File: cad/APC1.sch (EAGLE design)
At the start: 27 parts, among them IC1 LM555N, IC2 LM555N

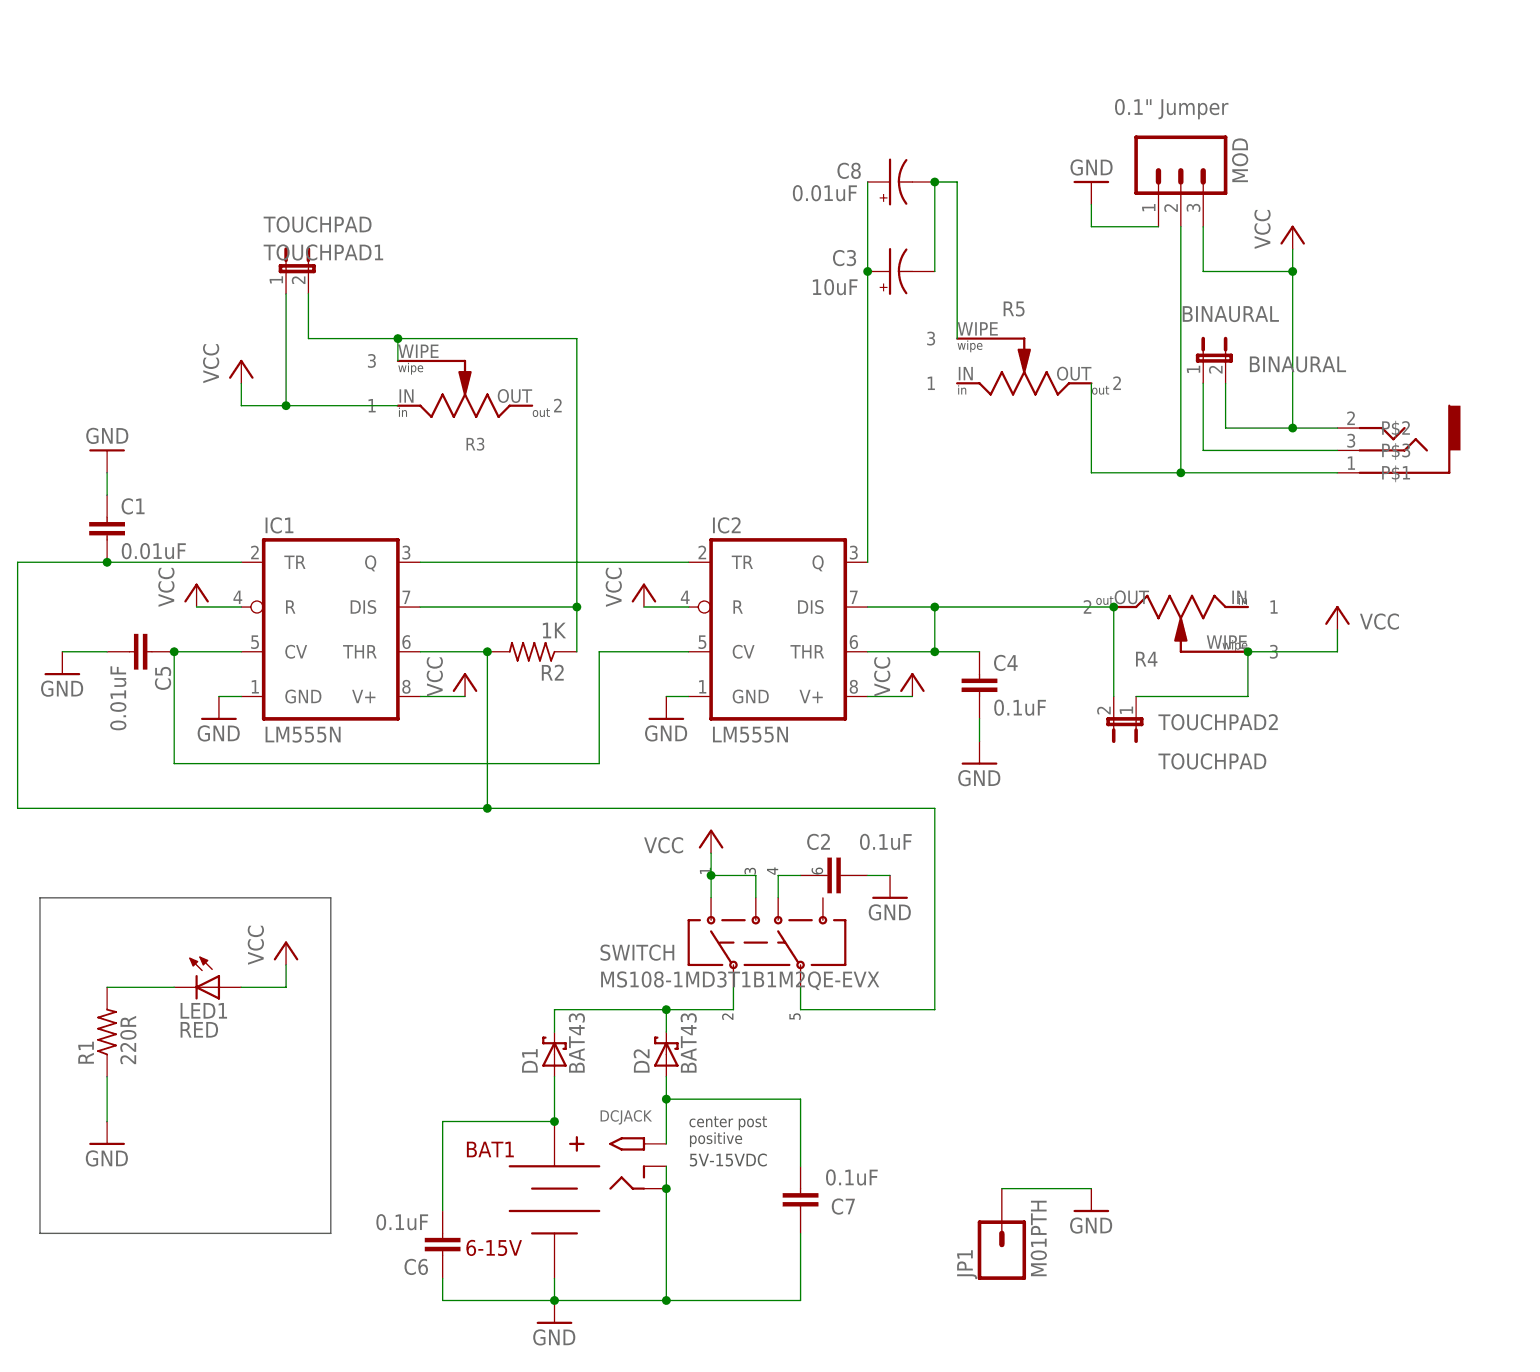
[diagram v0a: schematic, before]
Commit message: Fixed wiring on pots; more careful routing I had changed the schematic for two pots incorrectly, volume and pulse width. Added two current-limiting resistors for the freq. and pulse width pots. Spent more time with the trace routing. Eliminated a few vias. Widened trace widths and spread out traces to enable (at least potentially) desktop CNC PCB routing, such as with an OtherMill Pro. Changed some of the documentation and many of the images too, naturally. Also changed the .gitignore file to reflect more careful cataloging of the important parts of the project.
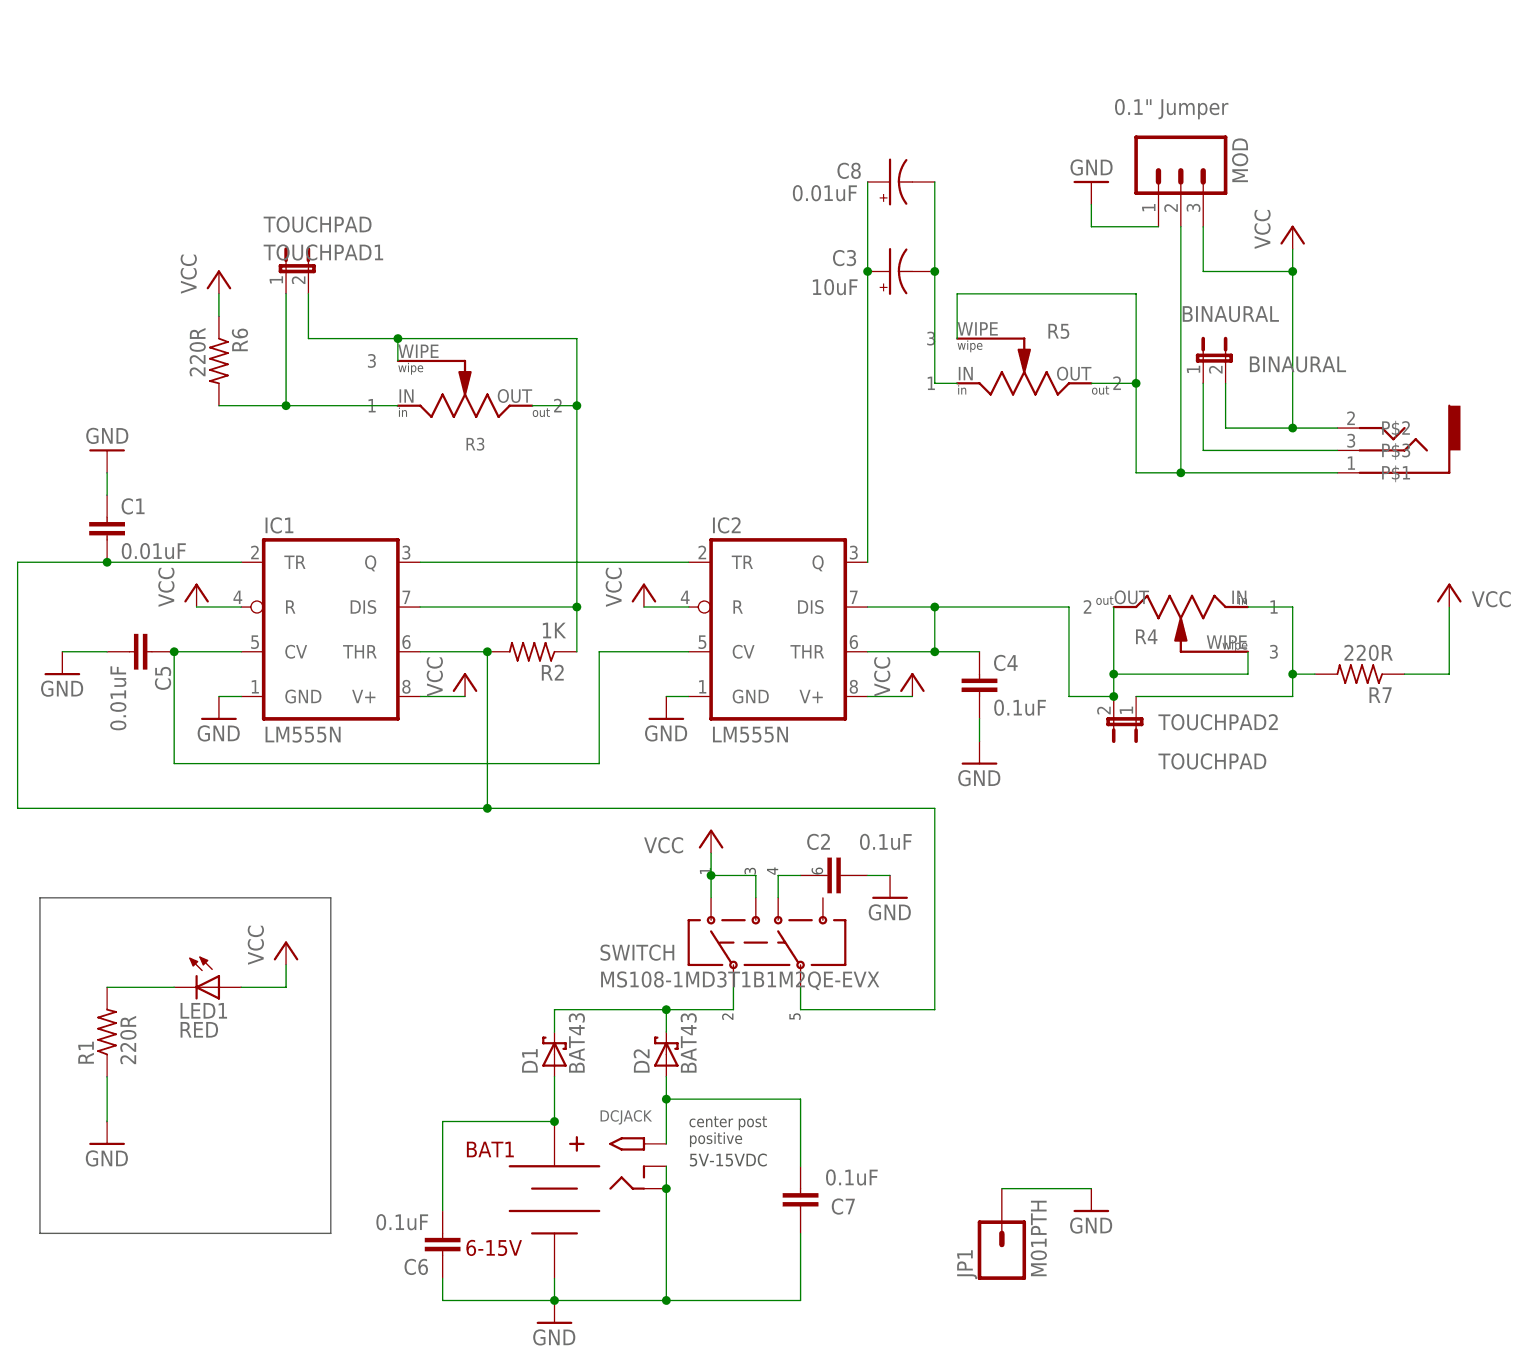
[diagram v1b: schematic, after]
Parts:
- added R6, R7: 220R, rcl:R-US_0207/7
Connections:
- new net N$13: LINE.P$1, MOD.2, R5.2, R5.3
- new net N$15: R3.1, R6.2, TOUCHPAD1.1
- net N$1: now also R3.2
- net N$14: now also R4.1, R7.2, TOUCHPAD2.1; no longer LINE.P$1, MOD.2, R5.2
- net N$16: now also R5.1; no longer R5.3
- net N$3: now also R4.3
- net VCC: now also R6.1, R7.1; no longer R3.1, R4.3, TOUCHPAD1.1, TOUCHPAD2.1
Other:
- note added: "Isolate from DC"
- note added: "These 220R resistors are probably unnecessary current-limiters in series with the rotary pots."
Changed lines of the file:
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@@
 <part name="JP1" library="SparkFun-Connectors" deviceset="M01" device="PTH"/>
 <part name="GND7" library="SparkFun-Aesthetics" deviceset="GND" device=""/>
+<part name="R6" library="rcl" deviceset="R-US_" device="0207/7" value="220R"/>
+<part name="R7" library="rcl" deviceset="R-US_" device="0207/7" value="220R"/>
 </parts>
 <sheets>
@@
 switch design that may
 be implemented later.</text>
+<text x="83.82" y="134.62" size="1.778" layer="98">Isolate from DC</text>
+<text x="5.08" y="132.08" size="1.778" layer="98" font="vector" ratio="10">These 220R resistors
+are probably unnecessary
+current-limiters in series
+with the rotary pots.</text>
 </plain>
 <instances>
@@
 <instance part="DCJACK" gate="G$1" x="66.04" y="17.78"/>
 <instance part="R5" gate="R$1" x="111.76" y="106.68" smashed="yes">
-<attribute name="NAME" x="109.22" y="114.3" size="1.6764" layer="95" font="vector"/>
+<attribute name="NAME" x="114.3" y="111.76" size="1.6764" layer="95" font="vector"/>
 <attribute name="VALUE" x="109.22" y="101.6" size="1.6764" layer="96" font="vector"/>
 </instance>
@@
 </instance>
 <instance part="R4" gate="R$1" x="129.54" y="81.28" smashed="yes" rot="R180">
-<attribute name="NAME" x="127" y="76.2" size="1.6764" layer="95" font="vector" rot="R180"/>
+<attribute name="NAME" x="127" y="78.74" size="1.6764" layer="95" font="vector" rot="R180"/>
 <attribute name="VALUE" x="132.08" y="86.36" size="1.6764" layer="96" font="vector" rot="R180"/>
 </instance>
 <instance part="P+1" gate="VCC" x="99.06" y="73.66"/>
 <instance part="P+2" gate="VCC" x="48.26" y="73.66"/>
-<instance part="P+3" gate="VCC" x="22.86" y="109.22"/>
+<instance part="P+3" gate="VCC" x="20.32" y="119.38"/>
 <instance part="GND1" gate="1" x="20.32" y="68.58"/>
 <instance part="GND2" gate="1" x="71.12" y="68.58"/>
-<instance part="P+4" gate="VCC" x="147.32" y="81.28" smashed="yes">
-<attribute name="VALUE" x="149.86" y="78.74" size="1.778" layer="96"/>
+<instance part="P+4" gate="VCC" x="160.02" y="83.82" smashed="yes">
+<attribute name="VALUE" x="162.56" y="81.28" size="1.778" layer="96"/>
 </instance>
 <instance part="GND3" gate="1" x="96.52" y="48.26"/>
@@
 <instance part="JP1" gate="G$1" x="109.22" y="7.62" rot="R90"/>
 <instance part="GND7" gate="1" x="119.38" y="12.7"/>
+<instance part="R6" gate="G$1" x="20.32" y="109.22" rot="R270"/>
+<instance part="R7" gate="G$1" x="149.86" y="73.66" rot="R180"/>
 </instances>
 <busses>
@@
 <pinref part="IC1" gate="A" pin="DIS"/>
 <wire x1="43.18" y1="81.28" x2="60.96" y2="81.28" width="0.1524" layer="91"/>
-<wire x1="60.96" y1="111.76" x2="60.96" y2="81.28" width="0.1524" layer="91"/>
+<wire x1="60.96" y1="111.76" x2="60.96" y2="104.14" width="0.1524" layer="91"/>
 <junction x="60.96" y="81.28"/>
 <pinref part="R3" gate="R$1" pin="3"/>
+<wire x1="60.96" y1="104.14" x2="60.96" y2="81.28" width="0.1524" layer="91"/>
 <wire x1="40.64" y1="109.22" x2="40.64" y2="111.76" width="0.1524" layer="91"/>
 <wire x1="40.64" y1="111.76" x2="60.96" y2="111.76" width="0.1524" layer="91"/>
@@
 <wire x1="30.48" y1="111.76" x2="40.64" y2="111.76" width="0.1524" layer="91"/>
 <junction x="40.64" y="111.76"/>
+<pinref part="R3" gate="R$1" pin="2"/>
+<wire x1="55.88" y1="104.14" x2="60.96" y2="104.14" width="0.1524" layer="91"/>
+<junction x="60.96" y="104.14"/>
 </segment>
 </net>
@@
 <segment>
 <pinref part="P+3" gate="VCC" pin="VCC"/>
-<pinref part="R3" gate="R$1" pin="1"/>
-<wire x1="22.86" y1="106.68" x2="22.86" y2="104.14" width="0.1524" layer="91"/>
-<wire x1="22.86" y1="104.14" x2="27.94" y2="104.14" width="0.1524" layer="91"/>
-<pinref part="TOUCHPAD1" gate="A" pin="1"/>
-<wire x1="27.94" y1="104.14" x2="40.64" y2="104.14" width="0.1524" layer="91"/>
-<wire x1="27.94" y1="116.84" x2="27.94" y2="104.14" width="0.1524" layer="91"/>
-<junction x="27.94" y="104.14"/>
+<wire x1="20.32" y1="116.84" x2="20.32" y2="114.3" width="0.1524" layer="91"/>
+<pinref part="R6" gate="G$1" pin="1"/>
 </segment>
 <segment>
 <pinref part="P+4" gate="VCC" pin="VCC"/>
-<pinref part="R4" gate="R$1" pin="3"/>
-<wire x1="137.16" y1="76.2" x2="147.32" y2="76.2" width="0.1524" layer="91"/>
-<wire x1="147.32" y1="76.2" x2="147.32" y2="78.74" width="0.1524" layer="91"/>
-<pinref part="TOUCHPAD2" gate="A" pin="1"/>
-<wire x1="124.46" y1="71.12" x2="137.16" y2="71.12" width="0.1524" layer="91"/>
-<wire x1="137.16" y1="71.12" x2="137.16" y2="76.2" width="0.1524" layer="91"/>
-<junction x="137.16" y="76.2"/>
+<pinref part="R7" gate="G$1" pin="1"/>
+<wire x1="154.94" y1="73.66" x2="160.02" y2="73.66" width="0.1524" layer="91"/>
+<wire x1="160.02" y1="73.66" x2="160.02" y2="81.28" width="0.1524" layer="91"/>
 </segment>
 <segment>
@@
 </segment>
 </net>
-<net name="N$14" class="0">
-<segment>
-<pinref part="LINE" gate="G$1" pin="P$1"/>
-<wire x1="129.54" y1="96.52" x2="119.38" y2="96.52" width="0.1524" layer="91"/>
-<wire x1="147.32" y1="96.52" x2="129.54" y2="96.52" width="0.1524" layer="91"/>
-<wire x1="129.54" y1="124.46" x2="129.54" y2="96.52" width="0.1524" layer="91"/>
-<junction x="129.54" y="96.52"/>
-<pinref part="MOD" gate="G$1" pin="2"/>
-<pinref part="R5" gate="R$1" pin="2"/>
-<wire x1="119.38" y1="96.52" x2="119.38" y2="106.68" width="0.1524" layer="91"/>
-</segment>
-</net>
 <net name="N$7" class="0">
 <segment>
@@
 <pinref part="IC2" gate="A" pin="DIS"/>
 <wire x1="93.98" y1="81.28" x2="101.6" y2="81.28" width="0.1524" layer="91"/>
-<junction x="101.6" y="81.28"/>
-<pinref part="R4" gate="R$1" pin="2"/>
-<wire x1="121.92" y1="81.28" x2="101.6" y2="81.28" width="0.1524" layer="91"/>
 <wire x1="101.6" y1="76.2" x2="101.6" y2="81.28" width="0.1524" layer="91"/>
 <junction x="101.6" y="76.2"/>
@@
 <pinref part="IC2" gate="A" pin="THR"/>
 <wire x1="93.98" y1="76.2" x2="101.6" y2="76.2" width="0.1524" layer="91"/>
+<wire x1="101.6" y1="81.28" x2="116.84" y2="81.28" width="0.1524" layer="91"/>
+<wire x1="116.84" y1="81.28" x2="116.84" y2="71.12" width="0.1524" layer="91"/>
+<junction x="101.6" y="81.28"/>
 <pinref part="TOUCHPAD2" gate="A" pin="2"/>
-<wire x1="121.92" y1="81.28" x2="121.92" y2="71.12" width="0.1524" layer="91"/>
-<junction x="121.92" y="81.28"/>
+<wire x1="116.84" y1="71.12" x2="121.92" y2="71.12" width="0.1524" layer="91"/>
+<pinref part="R4" gate="R$1" pin="3"/>
+<wire x1="137.16" y1="76.2" x2="137.16" y2="73.66" width="0.1524" layer="91"/>
+<wire x1="137.16" y1="73.66" x2="121.92" y2="73.66" width="0.1524" layer="91"/>
+<wire x1="121.92" y1="73.66" x2="121.92" y2="71.12" width="0.1524" layer="91"/>
+<junction x="121.92" y="71.12"/>
+<pinref part="R4" gate="R$1" pin="2"/>
+<wire x1="121.92" y1="81.28" x2="121.92" y2="73.66" width="0.1524" layer="91"/>
+<junction x="121.92" y="73.66"/>
 </segment>
 </net>
 <net name="N$16" class="0">
 <segment>
-<wire x1="104.14" y1="111.76" x2="104.14" y2="129.54" width="0.1524" layer="91"/>
 <pinref part="C3" gate="G$1" pin="-"/>
 <pinref part="C8" gate="G$1" pin="-"/>
-<junction x="101.6" y="129.54"/>
 <wire x1="101.6" y1="129.54" x2="101.6" y2="119.38" width="0.1524" layer="91"/>
-<wire x1="104.14" y1="129.54" x2="101.6" y2="129.54" width="0.1524" layer="91"/>
-<pinref part="R5" gate="R$1" pin="3"/>
+<wire x1="101.6" y1="119.38" x2="101.6" y2="106.68" width="0.1524" layer="91"/>
+<junction x="101.6" y="119.38"/>
+<pinref part="R5" gate="R$1" pin="1"/>
+<wire x1="101.6" y1="106.68" x2="104.14" y2="106.68" width="0.1524" layer="91"/>
 </segment>
 </net>
@@
 </segment>
 </net>
+<net name="N$13" class="0">
+<segment>
+<pinref part="R5" gate="R$1" pin="3"/>
+<wire x1="104.14" y1="111.76" x2="104.14" y2="116.84" width="0.1524" layer="91"/>
+<wire x1="104.14" y1="116.84" x2="124.46" y2="116.84" width="0.1524" layer="91"/>
+<wire x1="124.46" y1="116.84" x2="124.46" y2="106.68" width="0.1524" layer="91"/>
+<pinref part="LINE" gate="G$1" pin="P$1"/>
+<wire x1="124.46" y1="106.68" x2="124.46" y2="96.52" width="0.1524" layer="91"/>
+<wire x1="147.32" y1="96.52" x2="129.54" y2="96.52" width="0.1524" layer="91"/>
+<wire x1="129.54" y1="124.46" x2="129.54" y2="96.52" width="0.1524" layer="91"/>
+<pinref part="MOD" gate="G$1" pin="2"/>
+<wire x1="124.46" y1="96.52" x2="129.54" y2="96.52" width="0.1524" layer="91"/>
+<junction x="129.54" y="96.52"/>
+<pinref part="R5" gate="R$1" pin="2"/>
+<wire x1="119.38" y1="106.68" x2="124.46" y2="106.68" width="0.1524" layer="91"/>
+<junction x="124.46" y="106.68"/>
+</segment>
+</net>
+<net name="N$14" class="0">
+<segment>
+<pinref part="TOUCHPAD2" gate="A" pin="1"/>
+<wire x1="124.46" y1="71.12" x2="142.24" y2="71.12" width="0.1524" layer="91"/>
+<pinref part="R4" gate="R$1" pin="1"/>
+<wire x1="137.16" y1="81.28" x2="142.24" y2="81.28" width="0.1524" layer="91"/>
+<wire x1="142.24" y1="81.28" x2="142.24" y2="73.66" width="0.1524" layer="91"/>
+<pinref part="R7" gate="G$1" pin="2"/>
+<wire x1="142.24" y1="73.66" x2="142.24" y2="71.12" width="0.1524" layer="91"/>
+<wire x1="144.78" y1="73.66" x2="142.24" y2="73.66" width="0.1524" layer="91"/>
+<junction x="142.24" y="73.66"/>
+</segment>
+</net>
+<net name="N$15" class="0">
+<segment>
+<pinref part="R3" gate="R$1" pin="1"/>
+<wire x1="20.32" y1="104.14" x2="27.94" y2="104.14" width="0.1524" layer="91"/>
+<pinref part="TOUCHPAD1" gate="A" pin="1"/>
+<wire x1="27.94" y1="104.14" x2="40.64" y2="104.14" width="0.1524" layer="91"/>
+<wire x1="27.94" y1="116.84" x2="27.94" y2="104.14" width="0.1524" layer="91"/>
+<junction x="27.94" y="104.14"/>
+<pinref part="R6" gate="G$1" pin="2"/>
+</segment>
+</net>

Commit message: v.1.2 of board. Documentation changes / improvements.
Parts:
- removed C7: 0.1uF, rcl:C-EU050-024X044
- removed C8: 0.01uF, rcl:CPOL-USE2.5-7
- added FREQUENCY: M04X2, SparkFun-Connectors:M04X2
- added JP2: FREQ_BYPASS, SparkFun-Connectors:M03SMD_RA_MALE
- C6: value 0.1uF -> 0.01uF; device rcl:C-EU050-024X044 -> rcl:CPOL-USE2.5-7
- R1: value 220R -> 470R
- renumbered LED1 to LED
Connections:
- net N$12 renamed VIN
- new net N$18: FREQUENCY.1, R6.2
- new net N$19: FREQUENCY.4, JP2.1, R3.1
- new net N$20: FREQUENCY.6, IC1.DIS, R2.1
- net GND: now also FREQUENCY.7, FREQUENCY.8; no longer C6.1, C7.1
- net N$1: now also FREQUENCY.5, JP2.2, JP2.3; no longer IC1.DIS, R2.1
- net N$10: no longer C6.2
- net N$11: no longer C7.2
- net N$15: now also FREQUENCY.2, FREQUENCY.3; no longer R3.1, R6.2
- net N$16: now also C6.-; no longer C8.-
- net N$8: now also C6.+; no longer C8.+
